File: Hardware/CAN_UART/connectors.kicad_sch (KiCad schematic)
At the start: 6 parts, among them J1 CAN, J2 Conn_02x23_Odd_Even, J3 Conn_02x23_Odd_Even, J4 UART

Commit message: schematic update & pcb update
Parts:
- removed J1: CAN, symbol Connector:Screw_Terminal_01x02
- removed J2, J3: Conn_02x23_Odd_Even, PLC_STM_Power:PRT12790, symbol Connector_Generic:Conn_02x23_Odd_Even
- removed J4: UART, symbol Connector:Screw_Terminal_01x04
- added J2: UART, PLC_STM:1725656, symbol Connector:Screw_Terminal_01x02
- added J3: CAN, PLC_STM:1725656, symbol Connector:Screw_Terminal_01x02
- added J5: NUCLEO LEFT, PLC_STM:PRT12790, symbol Connector_Generic:Conn_02x23_Odd_Even
- added J6: NUCLEO RIGHT, PLC_STM:PRT12790, symbol Connector_Generic:Conn_02x23_Odd_Even
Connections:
- net +5V: now also J5.15 (Pin_15), J5.9 (Pin_9)
- net CAN.N: now also J3.2 (Pin_2)
- net CAN.P: now also J3.1 (Pin_1)
- net GND: now also J5.11 (Pin_11), J5.13 (Pin_13), J5.30 (Pin_30), J5.39 (Pin_39), J6.27 (Pin_27), J6.39 (Pin_39), J6.8 (Pin_8)
- net UART.RX: now also J2.1 (Pin_1)
- net UART.TX: now also J2.2 (Pin_2)
- new net +15V: J6.21 (Pin_21)
- new net +3V3: J5.7 (Pin_7)
- new net -15V: J5.18 (Pin_18)
- new net AGND: J6.25 (Pin_25)
- new net ANALOG_IN6: J6.12 (Pin_12)
- new net ANALOG_IN7: J6.14 (Pin_14)
- new net AO_0: J6.17 (Pin_17)
- new net AO_1: J6.10 (Pin_10)
- new net AVDD: J6.23 (Pin_23), J6.6 (Pin_6)
- new net CAN1_RX: J5.41 (Pin_41), J6.2 (Pin_2)
- new net CAN1_TX: J5.43 (Pin_43), J6.4 (Pin_4)
- new net CAN2_RX: J6.13 (Pin_13), J6.7 (Pin_7)
- new net CAN2_TX: J6.5 (Pin_5)
- new net UART2_RX: J5.22 (Pin_22)
- new net UART2_TX: J5.24 (Pin_24)
- new net UART4_RX: J5.8 (Pin_8)
- new net UART4_TX: J5.6 (Pin_6)
- new net UART5_RX: J5.12 (Pin_12), J6.46 (Pin_46)
- new net UART5_TX: J5.10 (Pin_10), J6.44 (Pin_44)
- new net UART6_RX: J6.42 (Pin_42)
- new net UART6_TX: J6.1 (Pin_1), J6.11 (Pin_11), J6.40 (Pin_40)
- no-connect marks 0 -> 56
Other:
- moved on the sheet: D1, D2

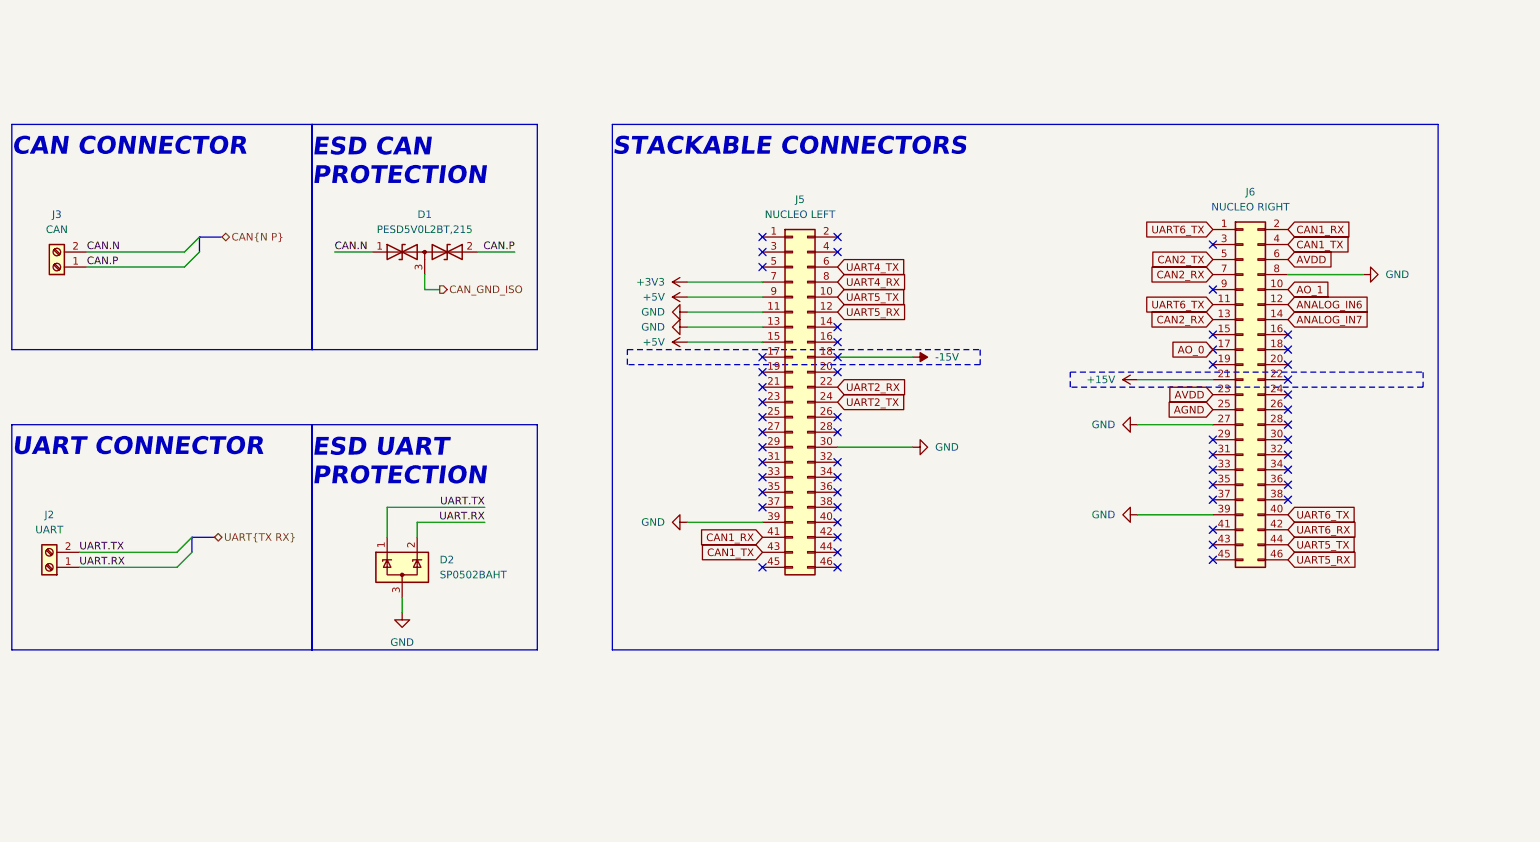
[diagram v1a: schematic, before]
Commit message: analog & can finished
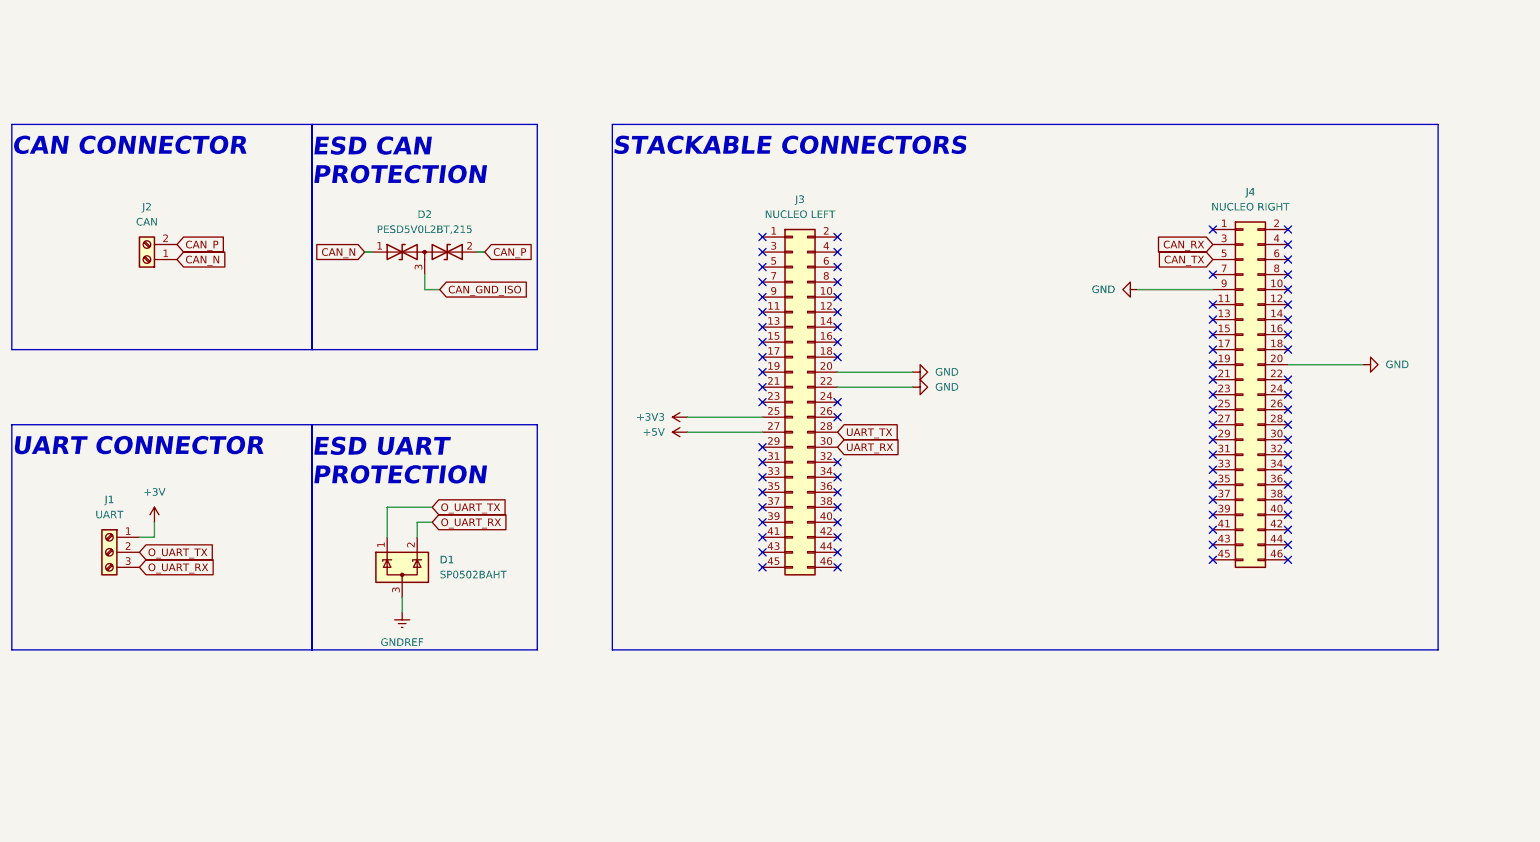
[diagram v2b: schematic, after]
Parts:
- removed J2: UART, PLC_STM:1725656, symbol Connector:Screw_Terminal_01x02
- added J1: UART, PLC_STM:1725669, symbol Connector:Screw_Terminal_01x03
- renumbered D2 to D1, D1 to D2, J3 to J2, J5 to J3, J6 to J4
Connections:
- net UART2_RX is gone; now on net GND: J3.22 (Pin_22)
- net +3V3: now also J3.25 (Pin_25); no longer J3.7 (Pin_7)
- net +5V: now also J3.27 (Pin_27); no longer J3.15 (Pin_15), J3.9 (Pin_9)
- net GND: now also J3.20 (Pin_20), J4.20 (Pin_20), J4.9 (Pin_9); no longer D1.3 (A), J3.11 (Pin_11), J3.13 (Pin_13), J3.30 (Pin_30), J3.39 (Pin_39), J4.27 (Pin_27), J4.39 (Pin_39), J4.8 (Pin_8)
- net CAN_RX: now reaches J4.3 (Pin_3)
- net UART_TX: now reaches J3.28 (Pin_28)
- net +15V: no longer names the net of J4.21 (Pin_21)
- net -15V: no longer names the net of J3.18 (Pin_18)
- net AGND: no longer names the net of J4.25 (Pin_25)
- net ANALOG_IN6: no longer names the net of J4.12 (Pin_12)
- net ANALOG_IN7: no longer names the net of J4.14 (Pin_14)
- net AO_0: no longer names the net of J4.17 (Pin_17)
- net AO_1: no longer names the net of J4.10 (Pin_10)
- net AVDD: no longer names the net of J4.23 (Pin_23)
- net AVDD: no longer J4.6 (Pin_6)
- net CAN.N renamed CAN_N
- net CAN_N: now also J2.1 (Pin_1); no longer J2.2 (Pin_2)
- net CAN.P renamed CAN_P
- net CAN_P: now also J2.2 (Pin_2); no longer J2.1 (Pin_1)
- net CAN1_RX: no longer names the net of J4.2 (Pin_2)
- net CAN1_RX: no longer J3.41 (Pin_41)
- net CAN1_TX: no longer names the net of J4.4 (Pin_4)
- net CAN1_TX: no longer J3.43 (Pin_43)
- net CAN2_RX: no longer names the net of J4.13 (Pin_13)
- net CAN2_RX: no longer J4.7 (Pin_7)
- net CAN2_TX renamed CAN_TX
- net UART.RX renamed O_UART_RX
- net O_UART_RX: now also J1.3 (Pin_3)
- net UART.TX renamed O_UART_TX
- net O_UART_TX: now also J1.2 (Pin_2)
- net UART2_TX: no longer names the net of J3.24 (Pin_24)
- net UART4_RX: no longer names the net of J3.8 (Pin_8)
- net UART4_TX: no longer names the net of J3.6 (Pin_6)
- net UART5_RX: no longer names the net of J4.46 (Pin_46)
- net UART5_RX: no longer J3.12 (Pin_12)
- net UART5_TX: no longer names the net of J4.44 (Pin_44)
- net UART5_TX: no longer J3.10 (Pin_10)
- net UART6_RX: no longer names the net of J4.42 (Pin_42)
- removed net UART6_TX: J4.1 (Pin_1), J4.11 (Pin_11), J4.40 (Pin_40)
- new net +3V: J1.1 (Pin_1)
- new net GNDREF: D1.3 (A)
- new net UART_RX: J3.30 (Pin_30)
- no-connect marks 56 -> 82
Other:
- moved on the sheet: J2
